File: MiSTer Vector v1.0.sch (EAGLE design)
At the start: 39 parts, among them CON2 22-23-2021, IC1 74HC00D, IC2 TL084, IC3 TL084, IC7 MAX6105, U1 MCP4922, U2 MCP4922, U3 MCP4922, U8 VASD1-SIP

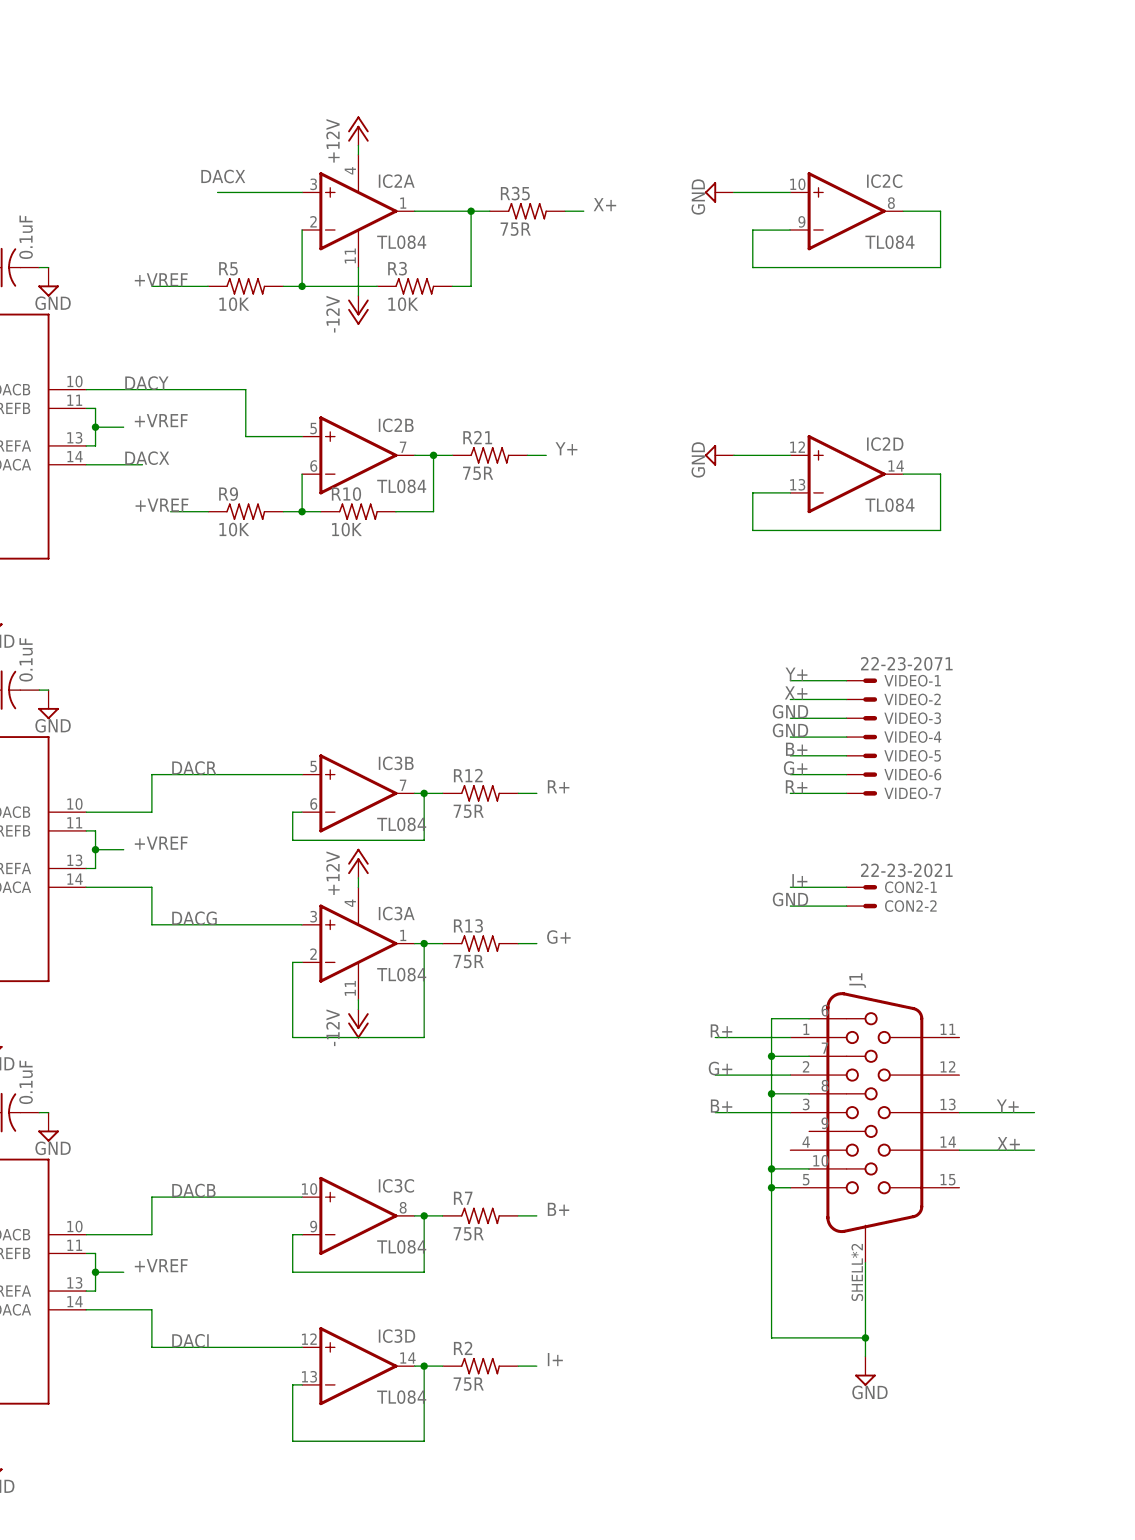
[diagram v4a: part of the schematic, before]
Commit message: changed DB15 to DB25, for use with laser projectors
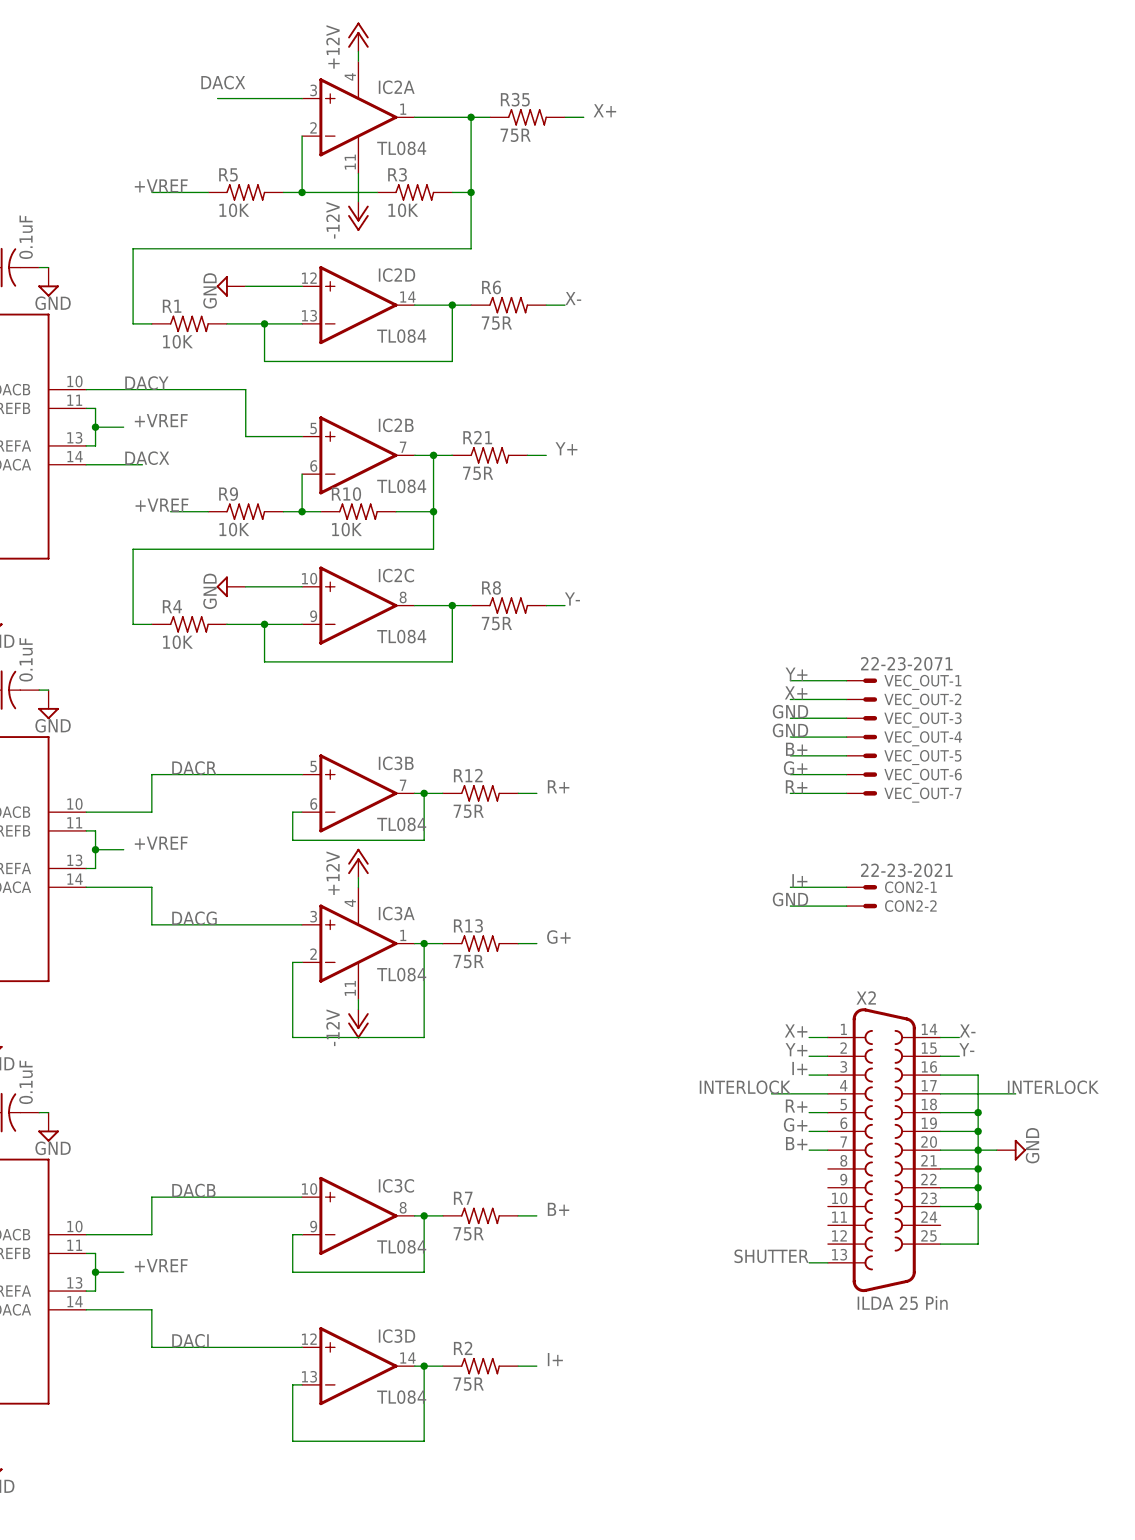
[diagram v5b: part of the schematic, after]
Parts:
- removed J1: (no value), con-wurth:618015330923
- added R1, R4: 10K, resistor:R-US_R0603
- added R6, R8: 75R, resistor:R-US_R0603
- added X2: ILDA 25 Pin, SparkFun:F25D
- renumbered VIDEO to VEC_OUT
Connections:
- new net INTERLOCK: X2.17, X2.4
- new net SHUTTER: X2.13
- new net X-: R6.2, X2.14
- new net Y-: R8.2, X2.15
- net B+: now also X2.7; no longer J1.3
- net G+: now also X2.6; no longer J1.2
- net GND: now also X2.16, X2.18, X2.19, X2.20, X2.21, X2.22, X2.23, X2.25; no longer J1.10, J1.5, J1.6, J1.7, J1.8, J1.SHIELD
- net I+: now also X2.3
- net N$1: now also R1.1
- net N$2: now also R4.1
- net N$4: now also R4.2, R8.1
- net N$5: now also R1.2, R6.1
- net R+: now also X2.5; no longer J1.1
- net X+: now also X2.1; no longer J1.14
- net Y+: now also X2.2; no longer J1.13
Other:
- moved on the sheet: IC2A, IC2C, IC2D, R3, R35, R5

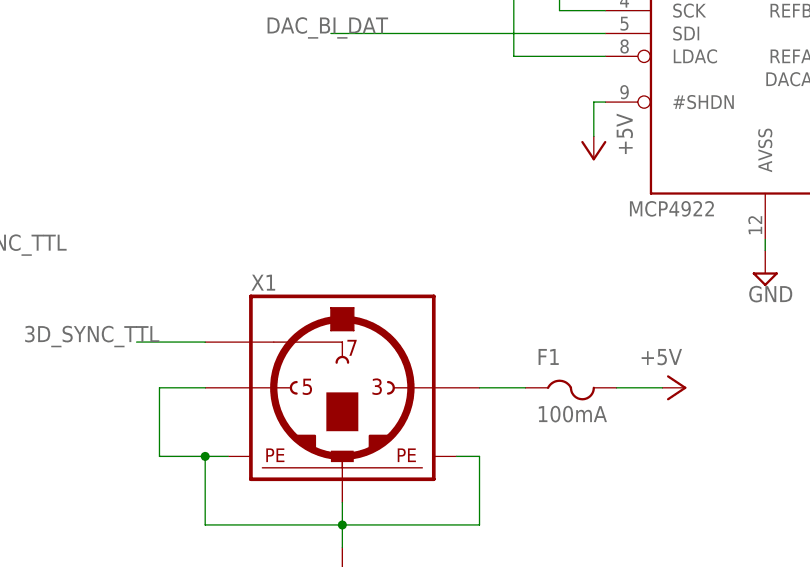
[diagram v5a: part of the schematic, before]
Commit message: made the PCB longer, to fit a specific project box
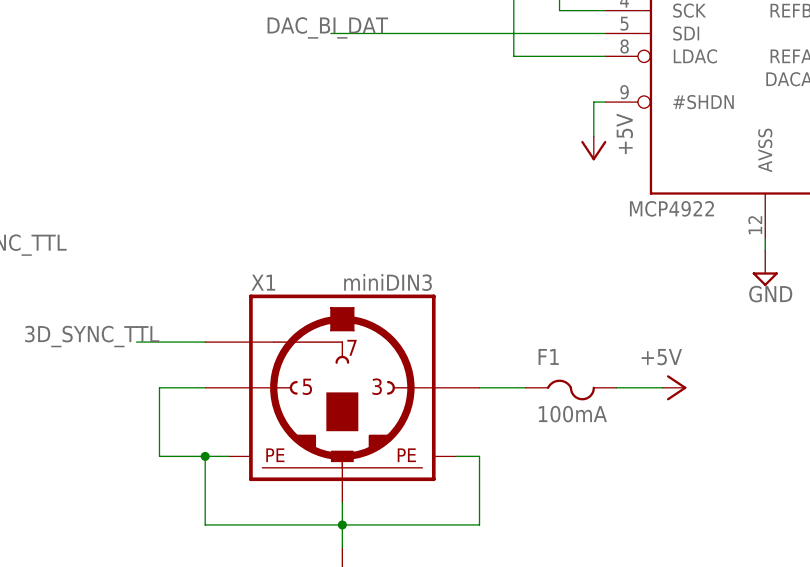
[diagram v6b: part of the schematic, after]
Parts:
- X1: value (none) -> miniDIN3
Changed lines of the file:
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@@
 <part name="SUPPLY13" library="supply2" deviceset="GND" device=""/>
 <part name="C11" library="adafruit" deviceset="C-US" device="C0603" value="0.1uF"/>
-<part name="X1" library="mini_din" deviceset="MINI_DIN_3" device=""/>
+<part name="X1" library="mini_din" deviceset="MINI_DIN_3" device="" value="miniDIN3"/>
 <part name="SUPPLY14" library="supply2" deviceset="GND" device=""/>
 <part name="P+14" library="supply1" deviceset="+5V" device=""/>

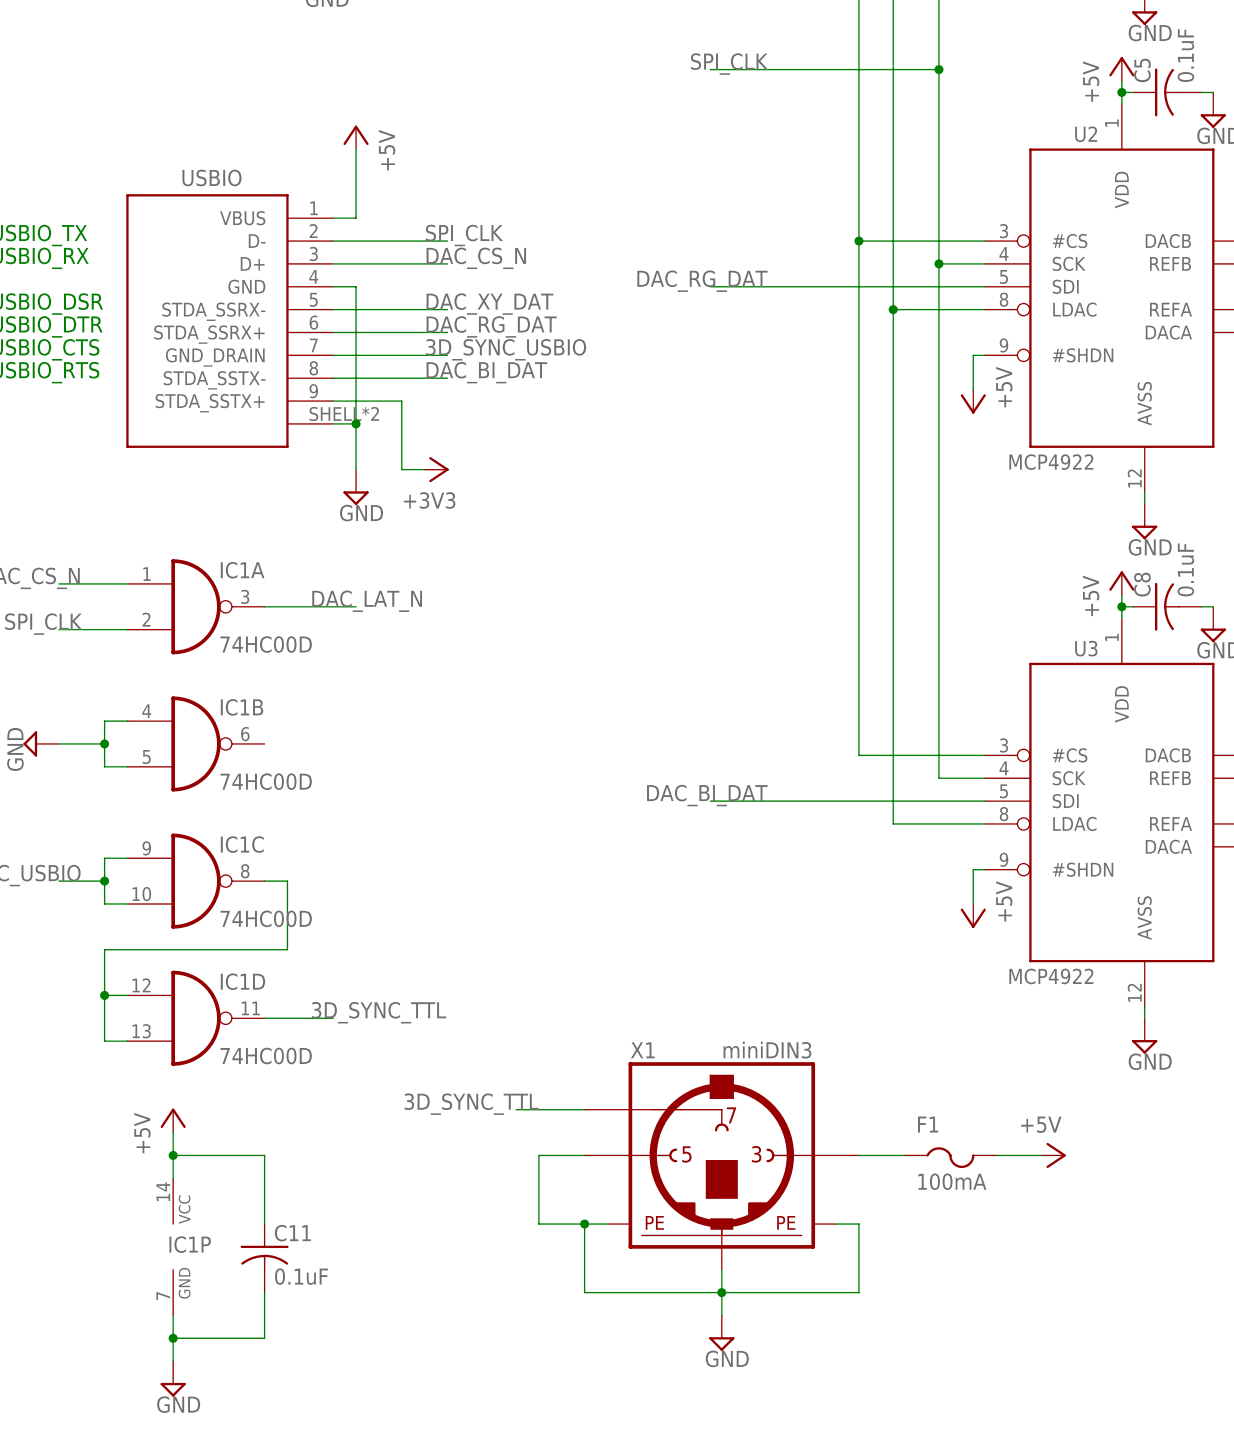
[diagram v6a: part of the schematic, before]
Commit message: changed the miniDIN for a miniUSB, to fit the case
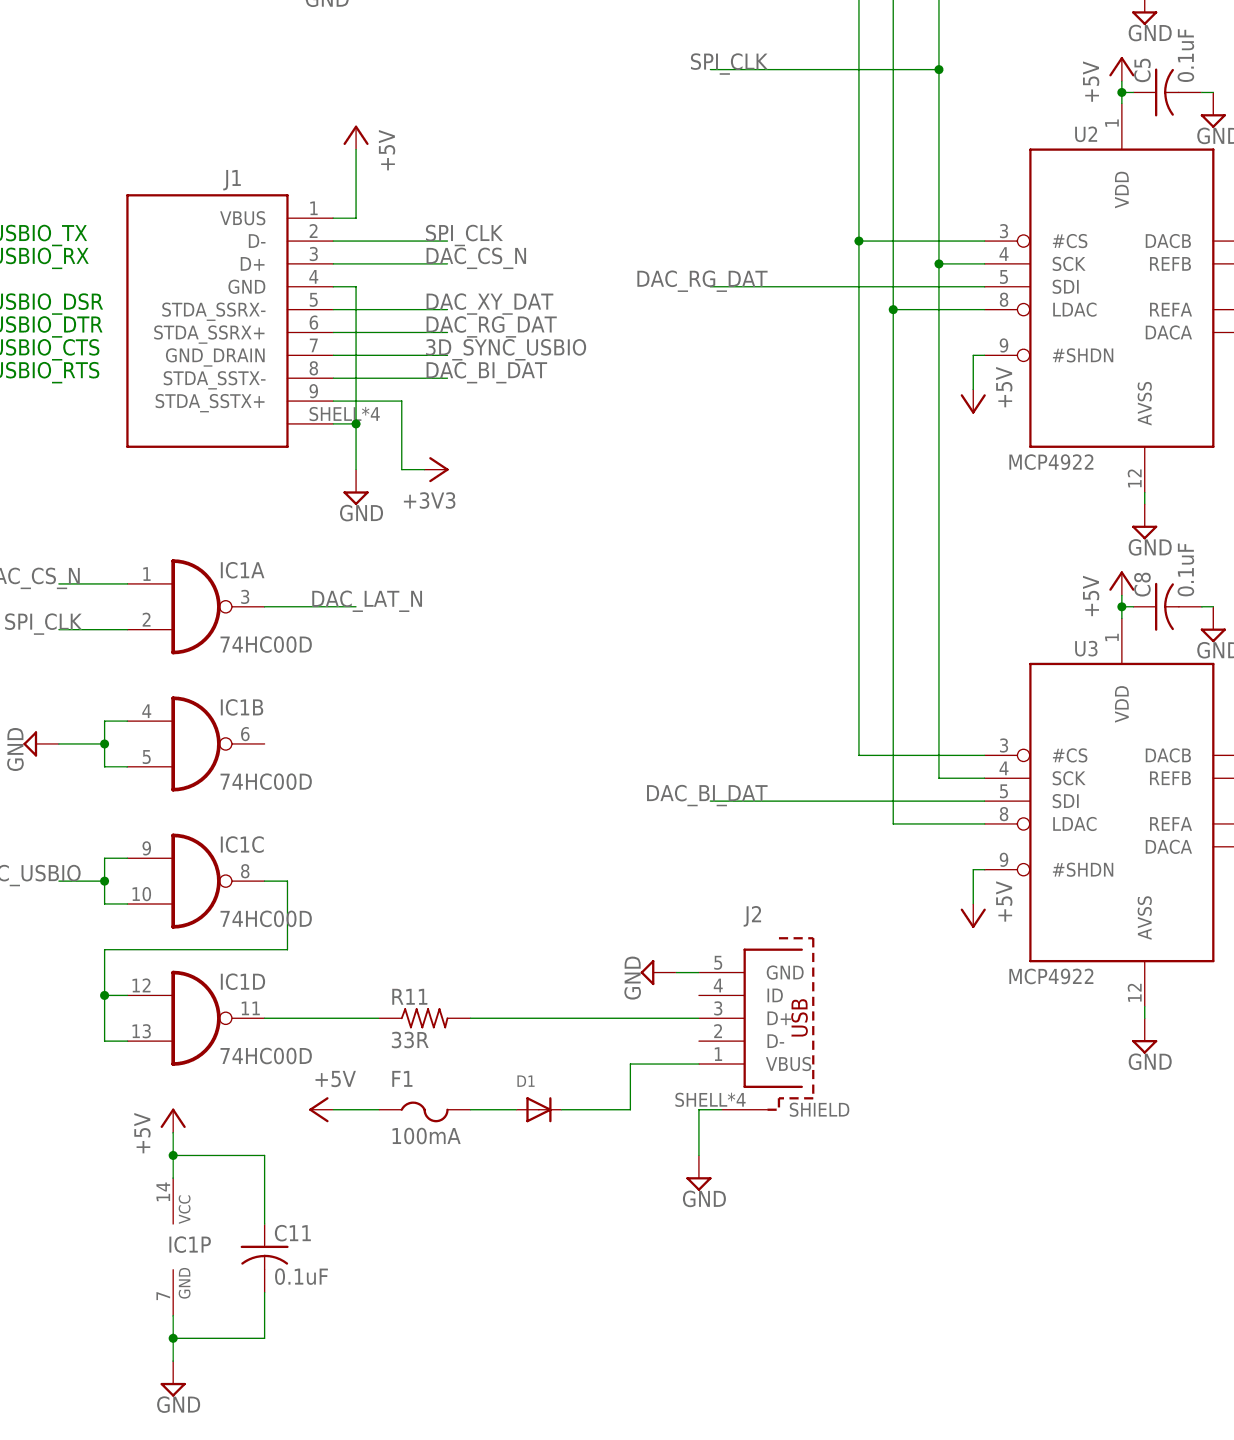
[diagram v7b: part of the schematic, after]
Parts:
- removed USBIO: (no value), con-wurth:692121030100
- removed X1: miniDIN3, mini_din:MINI_DIN_3
- added D1: (no value), adafruit:DIODESOD-323F
- added J1: (no value), 632723100011_Eagle_WR-USB_rev19b:692121230100
- added J2: (no value), 632723100011_Eagle_WR-USB_rev19b:65100516121
- added R11: 33R, resistor:R-US_R0603
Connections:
- removed net 3D_SYNC_TTL: IC1D.O, X1.7
- new net N$11: D1.A, F1.2
- new net N$7: IC1D.O, R11.1
- new net N$9: J2.D+, R11.2
- net +3V3: now also J1.STDA_SSTX+; no longer USBIO.STDA_SSTX+
- net +5V: now also F1.1, J1.VBUS; no longer F1.2, USBIO.VBUS
- net 3D_SYNC_USBIO: now also J1.GND_DRAIN; no longer USBIO.GND_DRAIN
- net DAC_BI_DAT: now also J1.STDA_SSTX-; no longer USBIO.STDA_SSTX-
- net DAC_CS_N: now also J1.D+; no longer USBIO.D+
- net DAC_RG_DAT: now also J1.STDA_SSRX+; no longer USBIO.STDA_SSRX+
- net DAC_XY_DAT: now also J1.STDA_SSRX-; no longer USBIO.STDA_SSRX-
- net GND: now also J1.GND, J1.SHIELD, J2.GND, J2.SHIELD; no longer USBIO.GND, USBIO.SHIELD, X1.5, X1.PE1, X1.PE2, X1.PE3
- net N$6: now also D1.C, J2.VBUS; no longer F1.1, X1.3
- net SPI_CLK: now also J1.D-; no longer USBIO.D-
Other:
- moved on the sheet: F1
